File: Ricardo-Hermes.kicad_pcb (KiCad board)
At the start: 4 copper layers, 43 x 65 mm, 151 parts, among them IC2 SX1280, J1 RBUS, J2 USB_C_Receptacle_USB2.0, J3 Conn_01x03_Pin, J4 Conn_01x03_Pin, U1 ESP32-S3, U11 SC4215ASTRT, U12 SKY66112-11, U2 SN65HVD230, U3 LM66200DRLR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

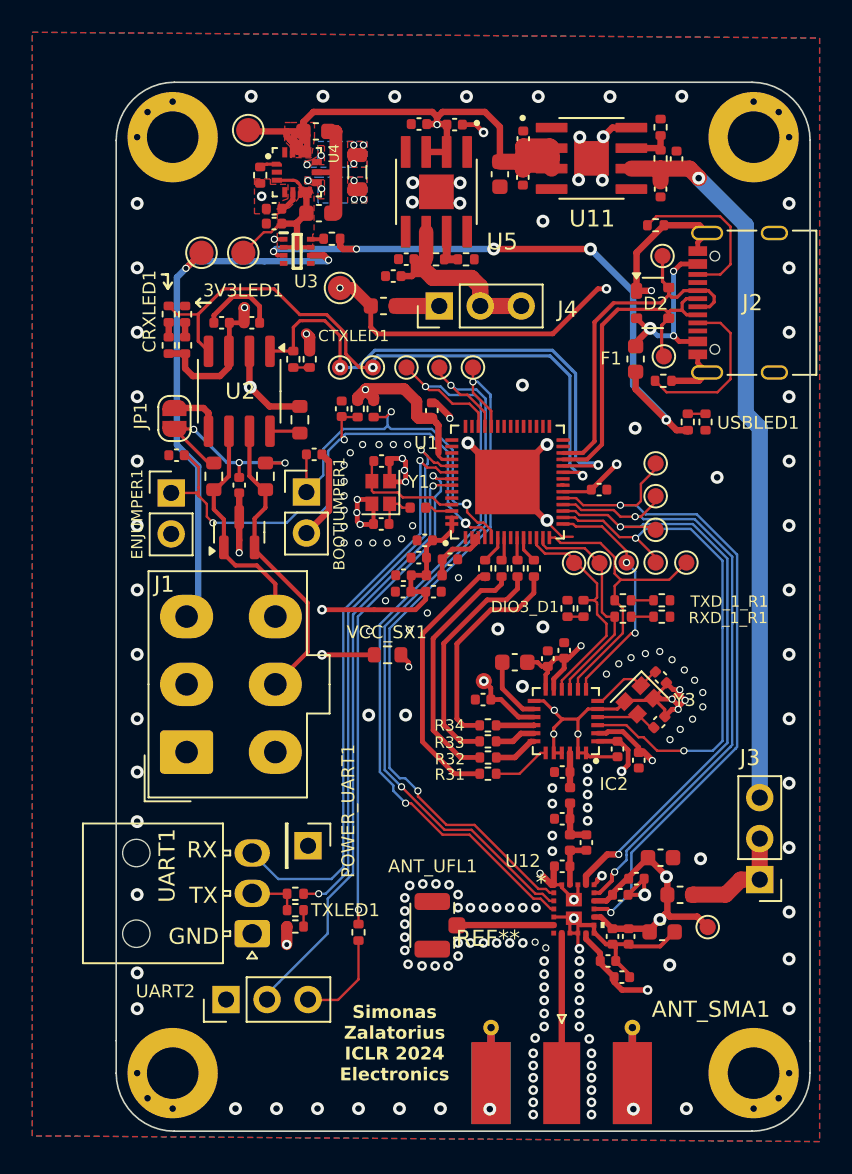
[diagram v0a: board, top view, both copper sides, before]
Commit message: Went for a 3v3 plane
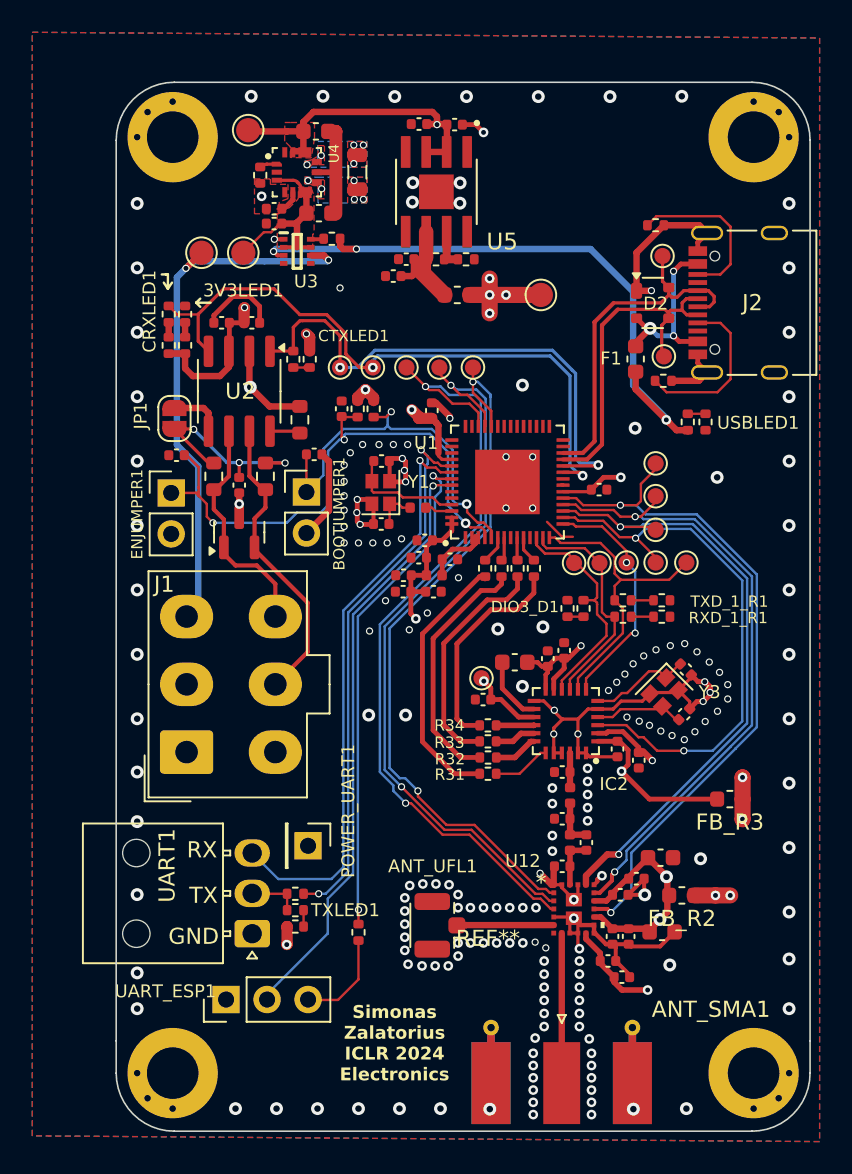
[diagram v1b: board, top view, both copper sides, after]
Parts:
- removed ?: , 
- removed C12: 22uF, Capacitor_SMD:C_0603_1608Metric
- removed C18, C62: 10uF, Capacitor_SMD:C_0402_1005Metric
- removed C19: 4.7uF, Capacitor_SMD:C_0402_1005Metric
- removed C64: 0.1uF, Capacitor_SMD:C_0402_1005Metric
- removed FB_R1: C3011209, Inductor_SMD:L_0603_1608Metric
- removed J3, J4: Conn_01x03_Pin, Connector_PinHeader_2.54mm:PinHeader_1x03_P2.54mm_Vertical
- removed R27: 56k, Resistor_SMD:R_0402_1005Metric
- removed R28: 10k, Resistor_SMD:R_0402_1005Metric
- removed U11: SC4215ASTRT, iclr:SOIC127P599X175-9N
- removed VCC_SX1: 0, Resistor_SMD:R_0603_1608Metric
- added FB_R2: C3011209, Inductor_SMD:L_0603_1608Metric, F.Cu at (153.3, 121.6)
- added FB_R3: C3011209, Inductor_SMD:L_0603_1608Metric, F.Cu at (156.2, 115.6)
- moved VAA_TP1 20.8 mm to (140.8, 108.1)
- moved 3V3_TP1 12.5 mm to (144.5, 84.4)
- moved FB_P1 4.62 mm to (139.3, 84.4), turned to 0 degrees
- moved C50 1.62 mm to (153.4, 110.3)
- moved Y3 1.62 mm to (152.2, 109.0)
- moved C51 1.62 mm to (153.5, 107.6)
- renumbered UART2 to UART_ESP1
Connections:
- C26 pad 2: Net-(J4-Pin_2) -> Net-(U5-VOUT)
- C27 pad 2: Net-(J4-Pin_2) -> Net-(U5-VOUT)
- C52 pad 1: VDDF -> +3V3
- C53 pad 1: VAA -> VPP
- C54 pad 1: VDDF -> +3V3
- C57 pad 1: VDDF -> +3V3
- C58 pad 1: VAA -> VPP
- FB_P1 pad 1: Net-(J4-Pin_1) -> Net-(U5-VOUT)
- IC2 pad 1: VAA -> VPP
- IC2 pad 11: VDDF -> +3V3
- IC2 pad 12: VDDF -> +3V3
- IC2 pad 15: VAA -> VPP
- IC2 pad 2: VDDF -> +3V3
- L4 pad 2: VDDF -> +3V3
- R16 pad 1: Net-(J4-Pin_2) -> Net-(U5-VOUT)
- U5 pad 6: Net-(J4-Pin_2) -> Net-(U5-VOUT)
- VAA_TP1 pad 1: VAA -> VPP
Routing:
- net +3V3: track 127.7 -> 56.7 mm, vias 9 -> 18
- net Net-(J3-Pin_3): track 45.2 -> 0.00 mm, vias 1 -> 0
- net VDDF: track 32.9 -> 0.00 mm, vias 3 -> 0
- net VAA: track 54.7 -> 25.1 mm, vias 5 -> 3
- net VPP: track 0.00 -> 25.7 mm, vias 0 -> 2
- net +VDC: track 40.5 -> 18.7 mm
- net Net-(J4-Pin_2): track 16.9 -> 0.00 mm
- net GND: track 336.3 -> 320.8 mm, vias 203 -> 206
- net Net-(U5-VOUT): track 0.00 -> 10.8 mm
- net Net-(J3-Pin_1): track 7.56 -> 0.00 mm
- net /RF Frontend/FBIn: track 2.78 -> 0.00 mm
- net Net-(J4-Pin_1): track 2.67 -> 0.00 mm
- net Net-(IC2-XTA): track 3.90 -> 5.65 mm
- net Net-(IC2-XTB): track 4.66 -> 6.40 mm
- net RF_RST: track 33.4 -> 34.4 mm
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- added copper zone on In2.Cu, net +3V3
- removed copper zone on In2.Cu, net GND

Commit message: Final changes and splitter prod files
splitter repo tbd
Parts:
- moved C1 0.63 mm to (137.3, 102.9)
- moved C4 0.63 mm to (135.4, 102.9)
- moved C5 0.63 mm to (135.4, 101.9)
- moved L1 0.63 mm to (137.3, 101.9)
- moved C7 0.57 mm to (136.4, 100.6)
- moved C6 0.47 mm to (139.3, 100.9)
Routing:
- net Net-(U1-MTDI/JTAG/GPIO41): track 34.0 -> 34.8 mm
- net GND: track 320.8 -> 320.4 mm, vias 206 -> 202
- net +3V3: track 56.7 -> 56.8 mm, vias 18 -> 19
- net +VDC: vias 1 -> 0

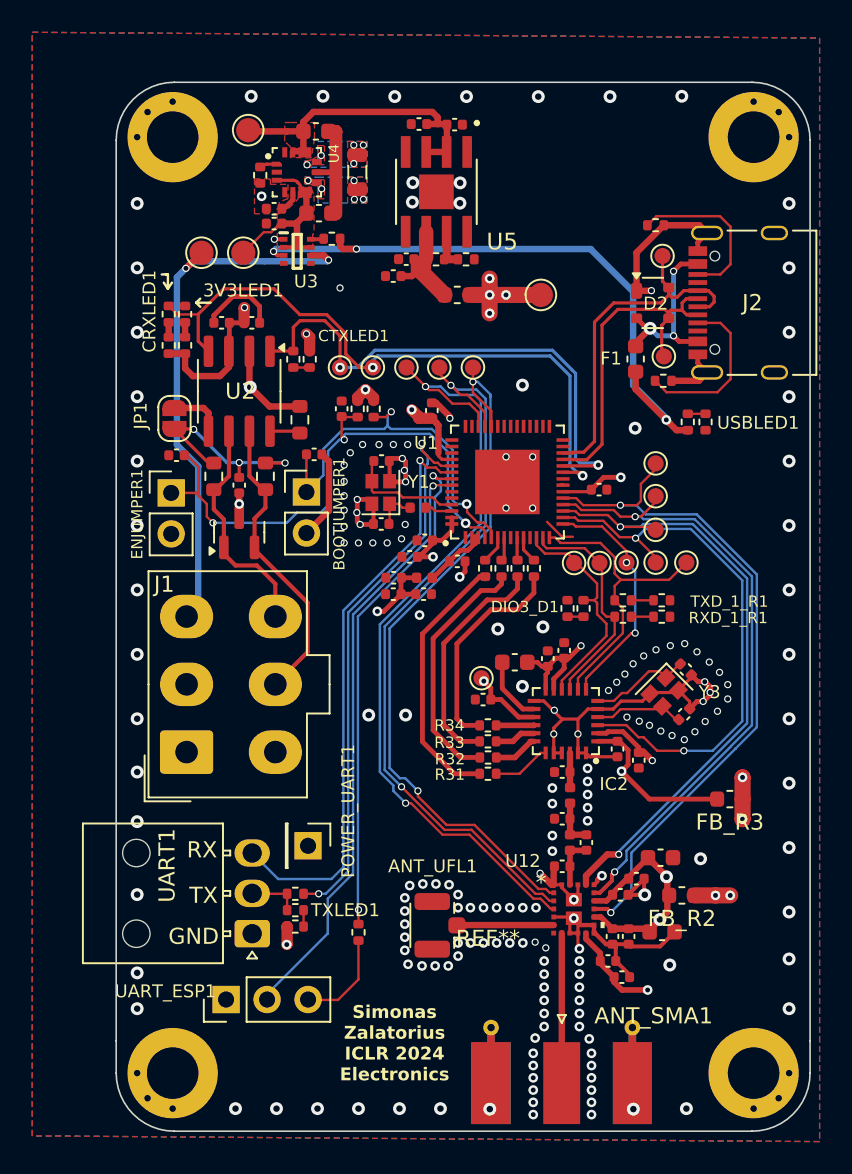
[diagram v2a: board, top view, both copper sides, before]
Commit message: New leds
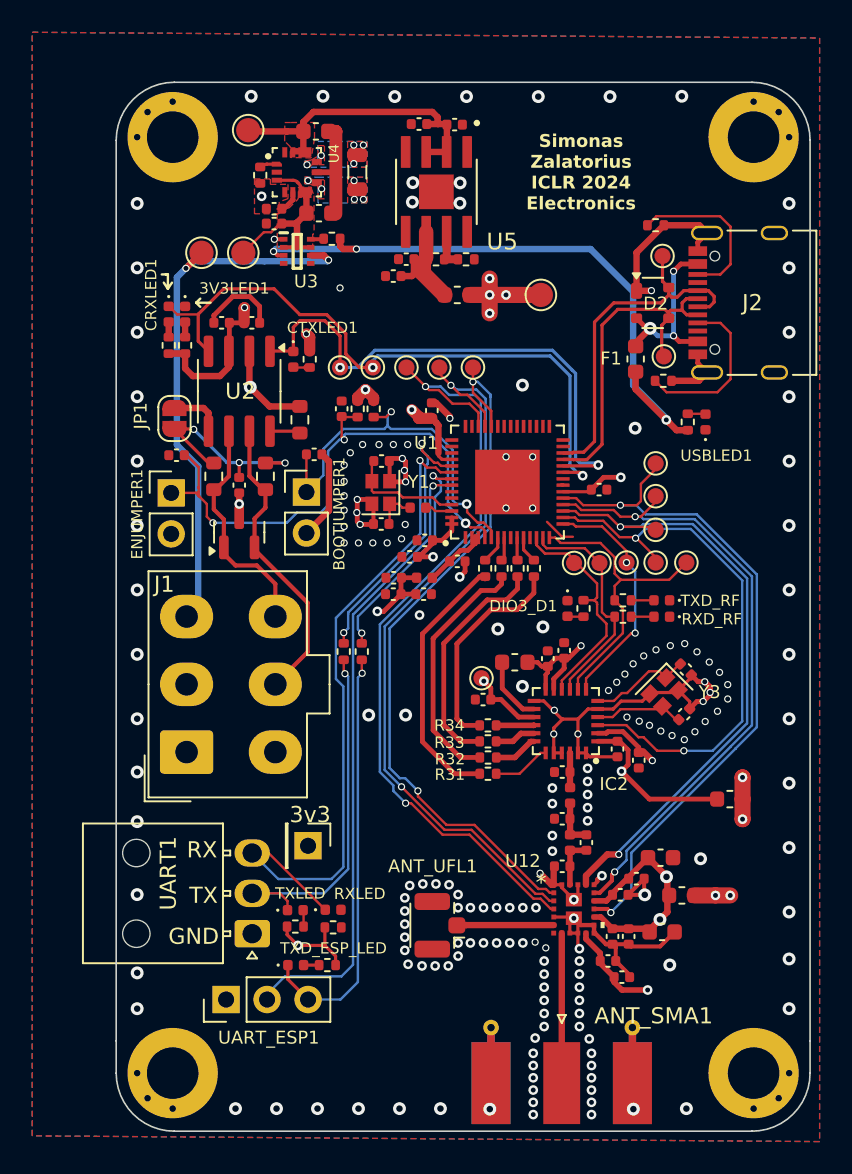
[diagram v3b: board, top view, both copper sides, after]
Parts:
- added R19: 470, Resistor_SMD:R_0402_1005Metric, F.Cu at (131.6, 123.6)
- added R20: 1k, Resistor_SMD:R_0402_1005Metric, F.Cu at (131.3, 125.9)
- added RXLED: GREEN_LED, Diode_SMD:D_0402_1005Metric, F.Cu at (131.6, 122.5)
- added TXD_ESP_LED: ORANGE_LED, Diode_SMD:D_0402_1005Metric, F.Cu at (129.3, 125.9)
- 3V3LED1, CRXLED1, CTXLED1, DIO3_D1, USBLED1: footprint Resistor_SMD:R_0402_1005Metric -> Diode_SMD:D_0402_1005Metric
- L4: footprint Capacitor_SMD:C_0603_1608Metric -> Inductor_SMD:L_0603_1608Metric
- RXD_RF: renamed from RXD_1_R1; footprint Resistor_SMD:R_0402_1005Metric -> Diode_SMD:D_0402_1005Metric
- TXD_RF: renamed from TXD_1_R1; footprint Resistor_SMD:R_0402_1005Metric -> Diode_SMD:D_0402_1005Metric
- TXLED: renamed from TXLED1; footprint Resistor_SMD:R_0402_1005Metric -> Diode_SMD:D_0402_1005Metric
- moved R6 17.4 mm to (133.4, 106.5)
- moved R7 15.3 mm to (132.3, 106.5), turned to 90 degrees
- renumbered POWER_UART1 to 3v3
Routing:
- net /TXD_ESP: track 6.07 -> 26.3 mm, vias 0 -> 1
- net /TXD: track 3.66 -> 23.1 mm, vias 0 -> 1
- net Net-(U1-MTDI/JTAG/GPIO41): track 34.8 -> 17.4 mm
- net Net-(U1-U0TXD/PROG/GPIO43): track 31.4 -> 14.1 mm
- net /RXD: track 36.1 -> 42.4 mm
- net +3V3: track 56.8 -> 61.5 mm
- net /RXD_ESP: track 37.3 -> 39.3 mm
- net Net-(CRXLED2-A): track 0.00 -> 0.97 mm

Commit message: Final fixes
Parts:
- removed RXLED, TXLED: GREEN_LED, Diode_SMD:D_0402_1005Metric
- added RXLED2: ORANGE_LED, Diode_SMD:D_0402_1005Metric, F.Cu at (131.7, 122.5)
- added TXLED1: GREEN_LED, Diode_SMD:D_0402_1005Metric, F.Cu at (129.3, 122.5)
- ESP_TX_LED1: renamed from TXD_ESP_LED; value ORANGE_LED -> GREEN_LED
- renumbered RXD_RF to RXD_1_RF, TXD_RF to TXD_1_RF
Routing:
- net Net-(RXLED2-A): track 0.00 -> 1.05 mm

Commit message: qr code
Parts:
- REF**: moved to B.Cu
- moved REF** 9.24 mm to (135.4, 130.3), turned to 180 degrees
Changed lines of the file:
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@@
 		(embedded_fonts no)
 	)
-	(footprint "Ky:Square_Of_Knowledge_QRCODE"
-		(layer "F.Cu")
-		(at 140.3828 122.5178)
-		(property "Reference" "REF**"
-			(at 0.8636 1.7272 0)
-			(unlocked yes)
-			(layer "F.SilkS")
-			(hide yes)
-			(effects
-				(font
-					(size 1 1)
-					(thickness 0.1)
-				)
-			)
-		)
-		(property "Value" "Square of knowledge"
-			(at 0 8.4 0)
-			(unlocked yes)
-			(layer "F.Fab")
-			(effects
-				(font
-					(size 1 1)
-					(thickness 0.15)
-				)
-			)
-		)
-		(property "Datasheet" ""
-			(at 0 0 0)
-			(unlocked yes)
-			(layer "F.Fab")
-			(hide yes)
-			(effects
-				(font
-					(size 1 1)
-					(thickness 0.15)
-				)
-			)
-		)
-		(property "Description" ""
-			(at 0 0 0)
-			(unlocked yes)
-			(layer "F.Fab")
-			(hide yes)
-			(effects
-				(font
-					(size 1 1)
-					(thickness 0.15)
-				)
-			)
-		)
-		(attr smd)
-		(fp_poly
-			(pts
-				(xy -5 -5) (xy 5 -5) (xy 5 5) (xy -5 5)
-			)
-			(stroke
-				(width 0.1)
-				(type solid)
-			)
-			(fill yes)
-			(layer "B.SilkS")
-		)
-		(fp_text user "${REFERENCE}"
-			(at 0 10.2 0)
-			(unlocked yes)
-			(layer "F.Fab")
-			(effects
-				(font
-					(size 1 1)
-					(thickness 0.15)
-				)
-			)
-		)
-		(embedded_fonts no)
-	)
 	(footprint "Capacitor_SMD:C_0402_1005Metric"
 		(layer "F.Cu")
@@
 		)
 		(embedded_fonts no)
+	)
+	(footprint "Ky:Square_Of_Knowledge_QRCODE"
+		(layer "B.Cu")
+		(at 135.379 130.2902 180)
+		(property "Reference" "REF**"
+			(at 0.8636 -1.7272 0)
+			(unlocked yes)
+			(layer "B.SilkS")
+			(hide yes)
+			(effects
+				(font
+					(size 1 1)
+					(thickness 0.1)
+				)
+				(justify mirror)
+			)
+		)
+		(property "Value" "Square of knowledge"
+			(at 0 -8.4 0)
+			(unlocked yes)
+			(layer "B.Fab")
+			(effects
+				(font
+					(size 1 1)
+					(thickness 0.15)
+				)
+				(justify mirror)
+			)
+		)
+		(property "Datasheet" ""
+			(at 0 0 0)
+			(unlocked yes)
+			(layer "B.Fab")
+			(hide yes)
+			(effects
+				(font
+					(size 1 1)
+					(thickness 0.15)
+				)
+				(justify mirror)
+			)
+		)
+		(property "Description" ""
+			(at 0 0 0)
+			(unlocked yes)
+			(layer "B.Fab")
+			(hide yes)
+			(effects
+				(font
+					(size 1 1)
+					(thickness 0.15)
+				)
+				(justify mirror)
+			)
+		)
+		(attr smd)
+		(fp_poly
+			(pts
+				(xy -2.5 2.5) (xy 2.5 2.5) (xy 2.5 -2.5) (xy -2.5 -2.5)
+			)
+			(stroke
+				(width 0.1)
+				(type solid)
+			)
+			(fill yes)
+			(layer "F.SilkS")
+		)
+		(fp_text user "${REFERENCE}"
+			(at 0 -10.2 0)
+			(unlocked yes)
+			(layer "B.Fab")
+			(effects
+				(font
+					(size 1 1)
+					(thickness 0.15)
+				)
+				(justify mirror)
+			)
+		)
+		(embedded_fonts no)
